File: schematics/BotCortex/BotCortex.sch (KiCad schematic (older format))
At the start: 60 parts, among them P1 2x Serial, P10 Stepper Upperarm, P11 Stepper Hip, P12 POWER_IN, P13 PowerEnableIn, P14 Power Stepper 2, P15 Power Stepper 3, P16 Power Stepper 4, P17 PowerEnableOut, P18 Power Stepper 5, P19 ODroid Power, P2 Herkulex Servo, P20 POTI 10K, P21 Reset_Conn, P22 Reset Conn, P23 LED-Driver-I2C, P24 UART6, P25 Thermal_Printer, P26 ResetTaster, P28 Power Stepper 1, P3 Encoder Socket 0, P4 Encoder Socket, P5 Stepper Elbow, P6 Power In uC Servo 9V, P7 Power Out uC Servo, P8 Stepper Forearm, P9 Stepper Wrist, Q1 BC237, Q2 BC237, SW2 reset, U1 7805, U2 LM7809ACT, U3 LM7809ACT, U4 Teensy_3.5

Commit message: fixed many bugs
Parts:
- P3: value Encoder Socket 0 -> Encoder Socket 1
- P4: value Encoder Socket -> Encoder Socket 0
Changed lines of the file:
@@
 P 4000 1150
 F 0 "P4" H 4000 1400 50  0000 C CNN
-F 1 "Encoder Socket" V 4100 1150 50  0000 C CNN
+F 1 "Encoder Socket 0" V 4100 1150 50  0000 C CNN
 F 2 "Connectors_Molex:Molex_KK_6410-04" H 4000 1150 60  0001 C CNN
 F 3 "" H 4000 1150 60  0000 C CNN
@@
 P 5200 1150
 F 0 "P3" H 5200 1400 50  0000 C CNN
-F 1 "Encoder Socket 0" V 5300 1150 50  0000 C CNN
+F 1 "Encoder Socket 1" V 5300 1150 50  0000 C CNN
 F 2 "Connectors_Molex:Molex_KK_6410-04" H 5200 1150 60  0001 C CNN
 F 3 "" H 5200 1150 60  0000 C CNN

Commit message: no message
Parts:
- added P23: LED driver, symbol CONN_01X05
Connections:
- net SCl1: now also P23.3 (P3); no longer P23.2 (P2), U4.29 (37/A18/PWM/SCL1)
- net SDA1: now also P23.2 (P2); no longer P23.3 (P3)

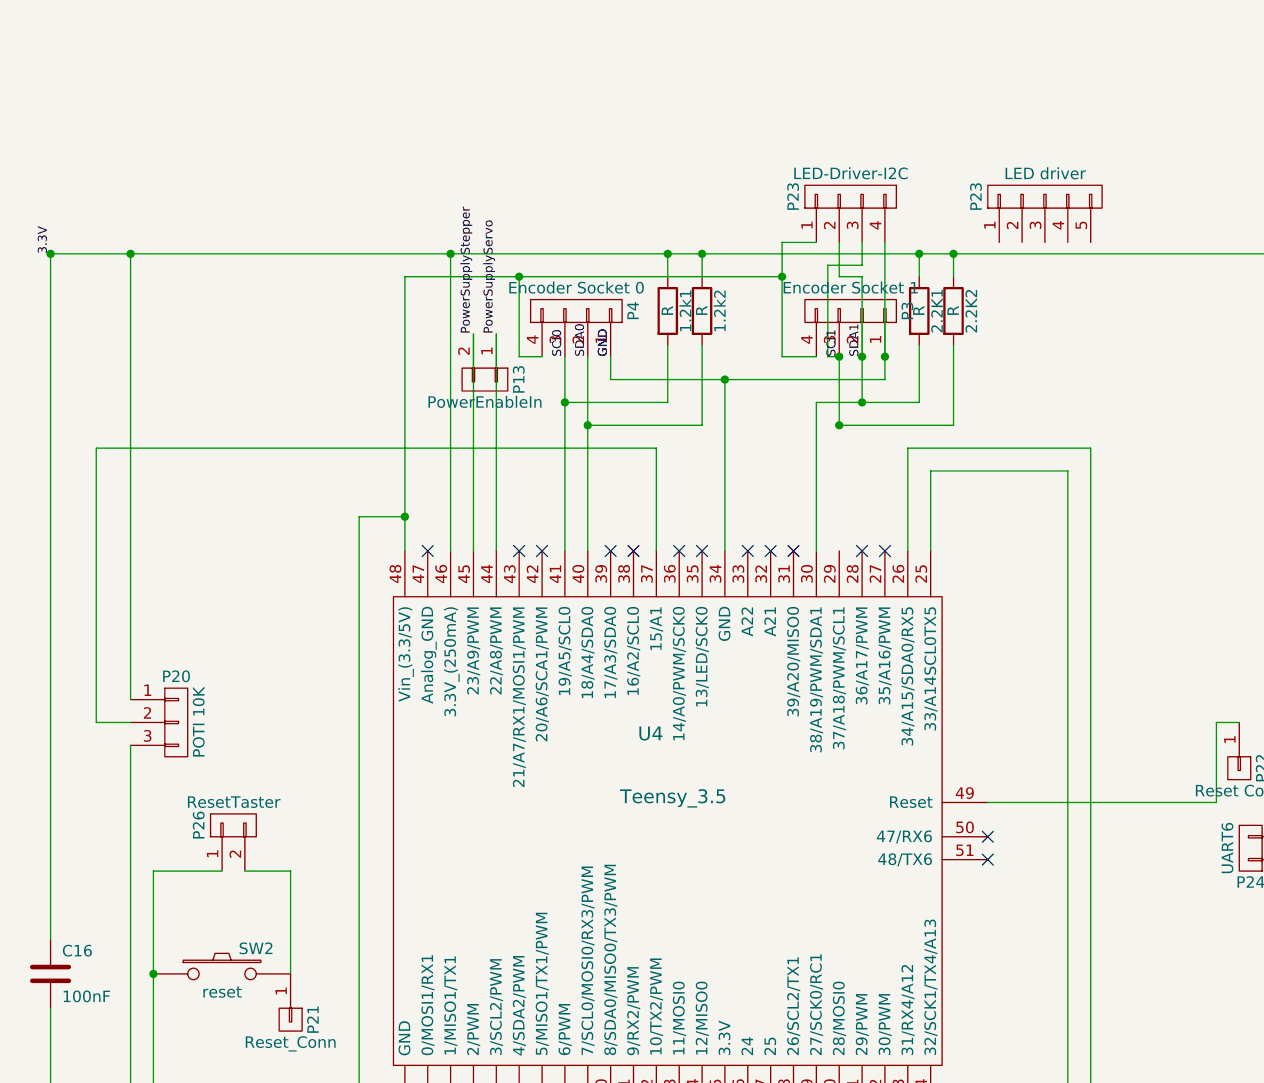
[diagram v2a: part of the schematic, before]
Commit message: added Reset LED to schematics and Cortex
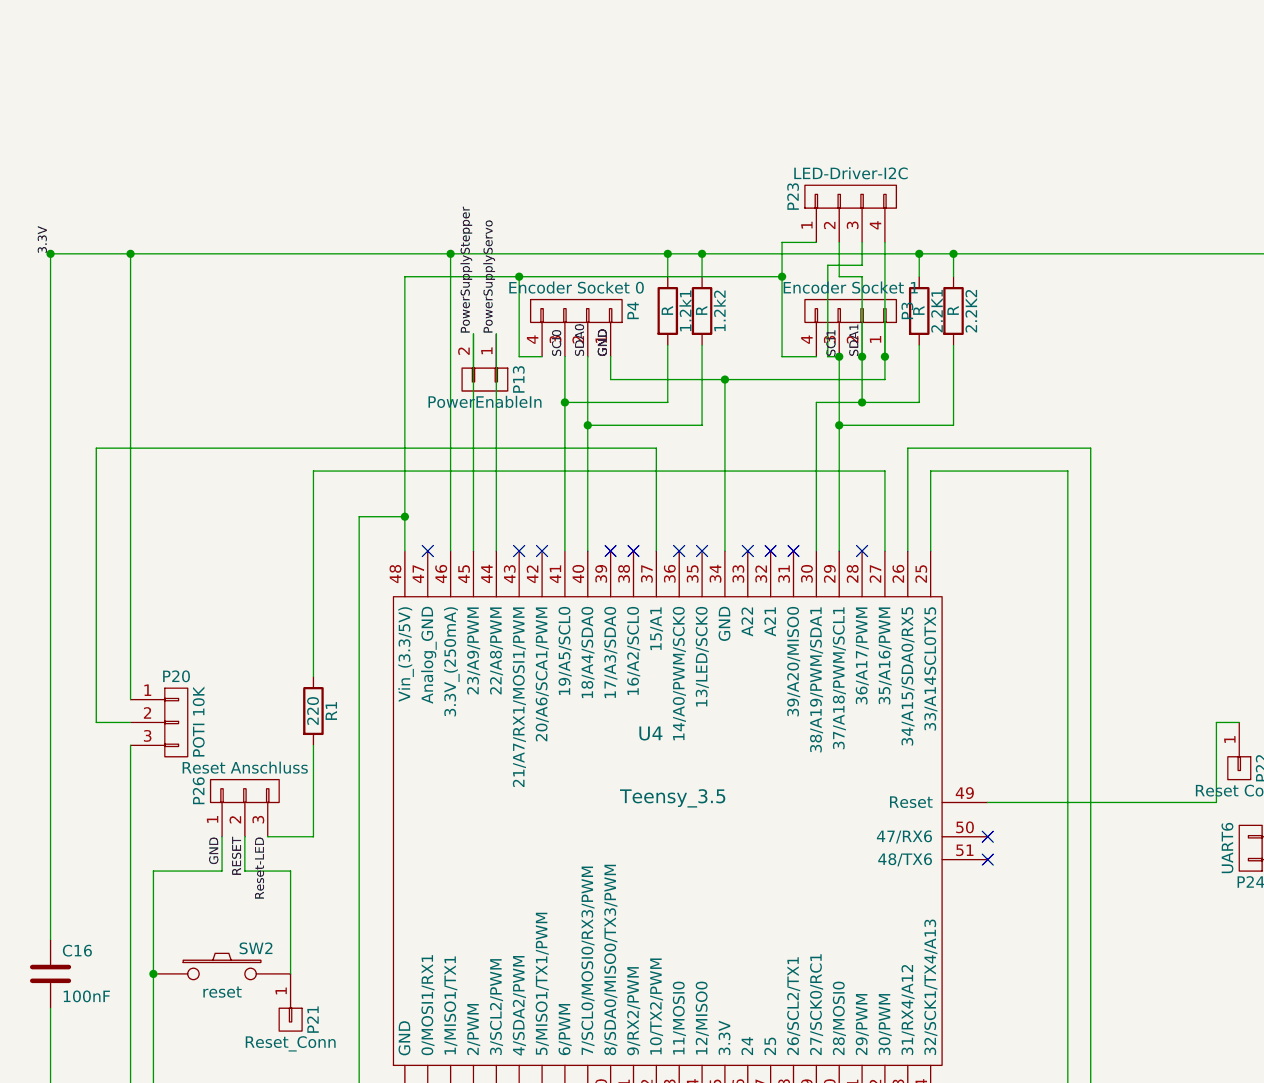
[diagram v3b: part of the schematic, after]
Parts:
- removed P23: LED driver, symbol CONN_01X05
- removed P26: ResetTaster, Connectors_Molex:Molex_KK_6410-02, symbol CONN_01X02
- added P26: Reset Anschluss, Connectors_Molex:Molex_KK_6410-03, symbol CONN_01X03
- added R1: 220, Discret:R4, symbol R
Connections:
- net GNDPWR: now also P26.1 (P1)
- net SCl1: now also U4.29 (37/A18/PWM/SCL1)
- net RESET: now reaches P21.1 (P1), SW2.2
- net RESET: now also P26.2 (P2)
- net at U4.27 (35/A16/PWM): now also R1.1
- new net Reset-LED: P26.3 (P3), R1.2
- no-connect marks 24 -> 23
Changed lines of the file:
@@
 NoConn ~ 4850 2200
 NoConn ~ 4950 2200
-NoConn ~ 5250 2200
-NoConn ~ 5350 2200
 Text Label 1700 900  1    39   ~ 0
 3.3V
@@
 	3750 1350 3750 1000
 Connection ~ 3750 1000
-$Comp
-L CONN_01X02 P26
-U 1 1 58618E53
-P 2500 3400
-F 0 "P26" H 2500 3550 50  0000 C CNN
-F 1 "ResetTaster" V 2600 3400 50  0000 C CNN
-F 2 "Connectors_Molex:Molex_KK_6410-02" H 2500 3400 50  0001 C CNN
-F 3 "" H 2500 3400 50  0000 C CNN
-	1    2500 3400
-	0    -1   -1   0
-$EndComp
 Wire Wire Line
 	2150 3600 2450 3600
@@
 	5250 950  5100 950
 Wire Wire Line
-	5150 1350 5150 1650
+	5150 1350 5150 2200
 Wire Wire Line
 	5150 1350 5100 1350
 Wire Wire Line
 	5100 1350 5100 950
-$Comp
-L CONN_01X05 P23
-U 1 1 587123EB
-P 6050 650
-F 0 "P23" H 6050 950 50  0000 C CNN
-F 1 "LED driver " V 6150 650 50  0000 C CNN
-F 2 "" H 6050 650 50  0000 C CNN
-F 3 "" H 6050 650 50  0000 C CNN
-	1    6050 650
-	0    -1   -1   0
-$EndComp
 Connection ~ 5150 1650
 $Comp
@@
 	0    -1   -1   0
 $EndComp
+$Comp
+L CONN_01X03 P26
+U 1 1 588D1F93
+P 2550 3250
+F 0 "P26" H 2550 3450 50  0000 C CNN
+F 1 "Reset Anschluss" V 2650 3250 50  0000 C CNN
+F 2 "Connectors_Molex:Molex_KK_6410-03" H 2550 3250 50  0001 C CNN
+F 3 "" H 2550 3250 50  0000 C CNN
+	1    2550 3250
+	0    -1   -1   0
+$EndComp
+Wire Wire Line
+	2450 3600 2450 3450
+Wire Wire Line
+	2550 3450 2550 3600
+$Comp
+L R R1
+U 1 1 588D29ED
+P 2850 2900
+F 0 "R1" V 2930 2900 50  0000 C CNN
+F 1 "220" V 2850 2900 50  0000 C CNN
+F 2 "Discret:R4" V 2780 2900 50  0001 C CNN
+F 3 "" H 2850 2900 50  0000 C CNN
+	1    2850 2900
+	1    0    0    -1
+$EndComp
+Wire Wire Line
+	2650 3450 2850 3450
+Wire Wire Line
+	2850 3450 2850 3050
+Wire Wire Line
+	2850 1850 2850 2750
+Wire Wire Line
+	2850 1850 5350 1850
+Wire Wire Line
+	5350 1850 5350 2200
+NoConn ~ 5250 2200
+Text Label 2450 3450 3    39   ~ 0
+GND
+Text Label 2550 3450 3    39   ~ 0
+RESET
+Text Label 2650 3450 3    39   ~ 0
+Reset-LED
 $EndSCHEMATC

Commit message: i2c pullup resistor reduced to 1.1K since i2c lines capacity was 400pF
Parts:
- renumbered 2.2K2 to 1.1K, 2.2K1 to 2.2K
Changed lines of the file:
@@
 $EndComp
 $Comp
-L R 2.2K1
+L R 2.2K
 U 1 1 58590BCF
 P 5500 1150
-F 0 "2.2K1" V 5580 1150 50  0000 C CNN
+F 0 "2.2K" V 5580 1150 50  0000 C CNN
 F 1 "R" V 5500 1150 50  0000 C CNN
 F 2 "Discret:R4" V 5430 1150 50  0001 C CNN
@@
 $EndComp
 $Comp
-L R 2.2K2
+L R 1.1K
 U 1 1 58590D16
 P 5650 1150
-F 0 "2.2K2" V 5730 1150 50  0000 C CNN
+F 0 "1.1K" V 5730 1150 50  0000 C CNN
 F 1 "R" V 5650 1150 50  0000 C CNN
 F 2 "Discret:R4" V 5580 1150 50  0001 C CNN

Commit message: Weekend
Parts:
- P19: value ODroid Power -> Thermal Printer 5V
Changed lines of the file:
@@
 P 1550 10100
 F 0 "P19" H 1550 10250 50  0000 C CNN
-F 1 "ODroid Power" V 1650 10100 50  0000 C CNN
+F 1 "Thermal Printer 5V" V 1650 10100 50  0000 C CNN
 F 2 "Connect:bornier2" H 1550 10100 50  0001 C CNN
 F 3 "" H 1550 10100 50  0000 C CNN

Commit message: reduced pullup resistors in I2C lines
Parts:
- renumbered 2.2K to 1.2K1, 1.1K to 1.2K2
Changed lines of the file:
@@
 DIR4
 $Comp
-L GNDPWR #PWR01
+L GNDPWR #PWR2
 U 1 1 576CFF3F
 P 1200 7800
-F 0 "#PWR01" H 1200 7600 50  0001 C CNN
+F 0 "#PWR2" H 1200 7600 50  0001 C CNN
 F 1 "GNDPWR" H 1200 7670 50  0000 C CNN
 F 2 "" H 1200 7750 60  0000 C CNN
@@
 $EndComp
 $Comp
-L PWR_FLAG #FLG02
+L PWR_FLAG #FLG2
 U 1 1 576CF103
 P 1000 7150
-F 0 "#FLG02" H 1000 7245 50  0001 C CNN
+F 0 "#FLG2" H 1000 7245 50  0001 C CNN
 F 1 "PWR_FLAG" H 1000 7330 50  0000 C CNN
 F 2 "" H 1000 7150 60  0000 C CNN
@@
 $EndComp
 $Comp
-L GNDPWR #PWR03
+L GNDPWR #PWR1
 U 1 1 577CA6B0
 P 950 10800
-F 0 "#PWR03" H 950 10600 50  0001 C CNN
+F 0 "#PWR1" H 950 10600 50  0001 C CNN
 F 1 "GNDPWR" H 950 10670 50  0000 C CNN
 F 2 "" H 950 10750 60  0000 C CNN
@@
 $EndComp
 $Comp
-L PWR_FLAG #FLG04
+L PWR_FLAG #FLG1
 U 1 1 577CA6B1
 P 950 8600
-F 0 "#FLG04" H 950 8695 50  0001 C CNN
+F 0 "#FLG1" H 950 8695 50  0001 C CNN
 F 1 "PWR_FLAG" H 950 8780 50  0000 C CNN
 F 2 "" H 950 8600 60  0000 C CNN
@@
 $EndComp
 $Comp
-L PWR_FLAG #FLG05
+L PWR_FLAG #FLG3
 U 1 1 576D01C9
 P 1200 7800
-F 0 "#FLG05" H 1200 7895 50  0001 C CNN
+F 0 "#FLG3" H 1200 7895 50  0001 C CNN
 F 1 "PWR_FLAG" H 1200 7980 50  0000 C CNN
 F 2 "" H 1200 7800 60  0000 C CNN
@@
 $EndComp
 $Comp
-L R 2.2K
+L R 1.2K1
 U 1 1 58590BCF
 P 5500 1150
-F 0 "2.2K" V 5580 1150 50  0000 C CNN
+F 0 "1.2K1" V 5580 1150 50  0000 C CNN
 F 1 "R" V 5500 1150 50  0000 C CNN
 F 2 "Discret:R4" V 5430 1150 50  0001 C CNN
@@
 $EndComp
 $Comp
-L R 1.1K
+L R 1.2K2
 U 1 1 58590D16
 P 5650 1150
-F 0 "1.1K" V 5730 1150 50  0000 C CNN
+F 0 "1.2K2" V 5730 1150 50  0000 C CNN
 F 1 "R" V 5650 1150 50  0000 C CNN
 F 2 "Discret:R4" V 5580 1150 50  0001 C CNN
